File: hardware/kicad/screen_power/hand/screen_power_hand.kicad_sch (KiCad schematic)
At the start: 12 parts, among them J1 AUX 5V INPUT, J2 SCREEN CONTROL, Q1 2N3904

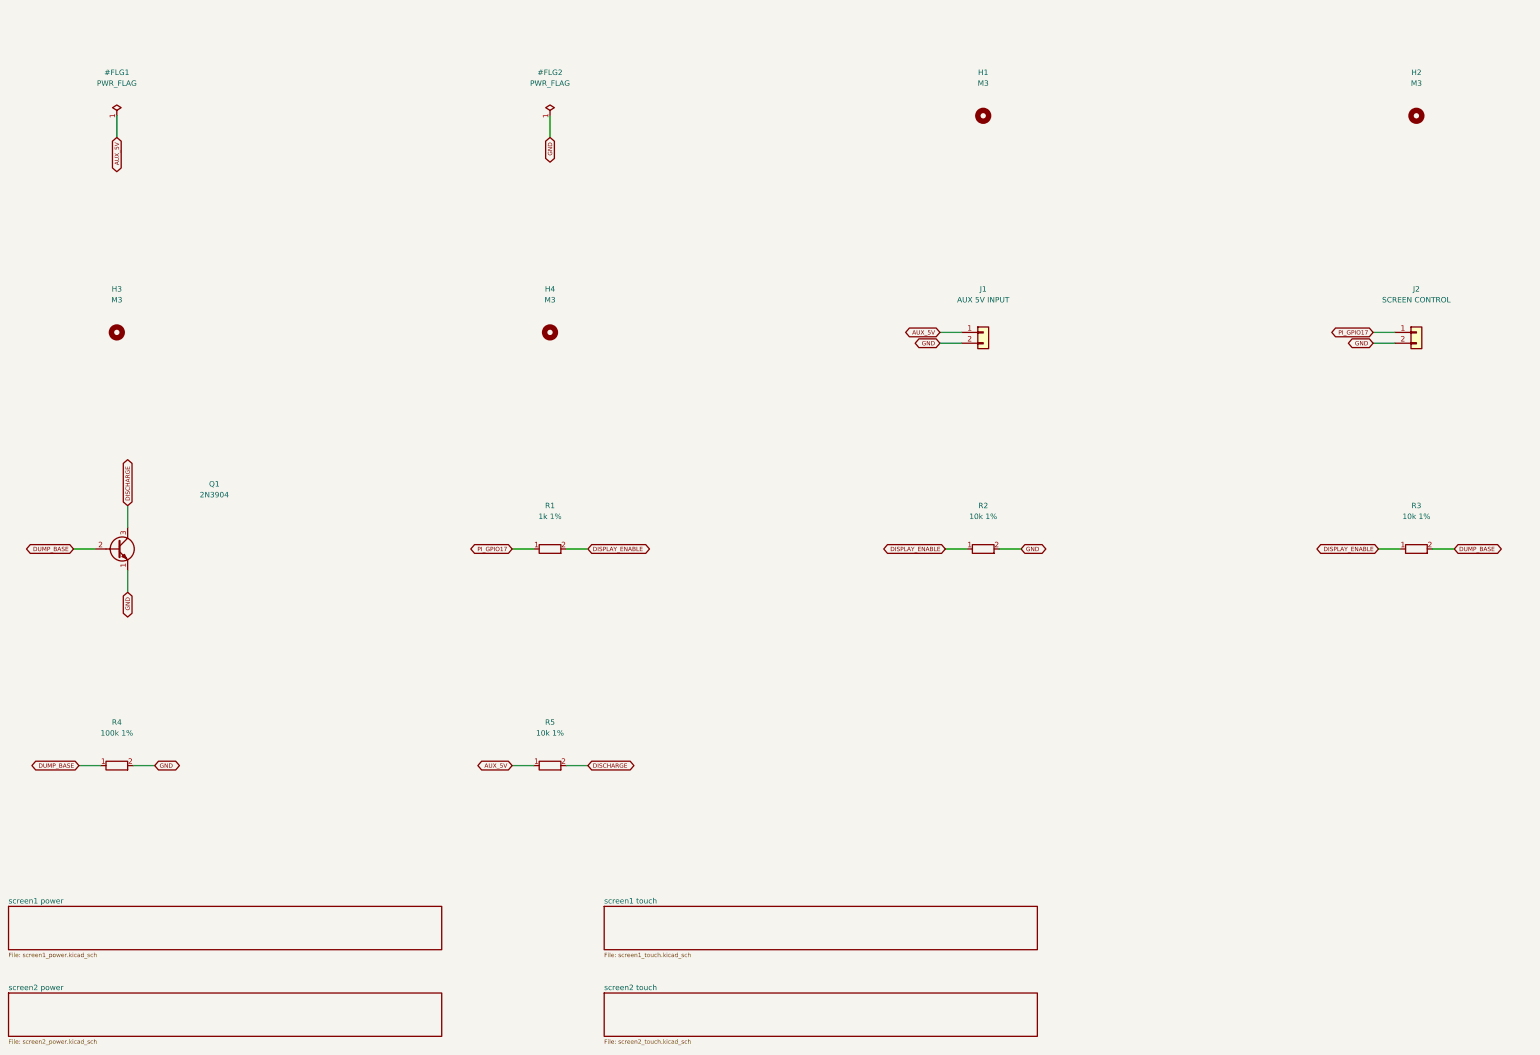
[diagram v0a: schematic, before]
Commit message: refactor(hardware): simplify and compact screen power boards
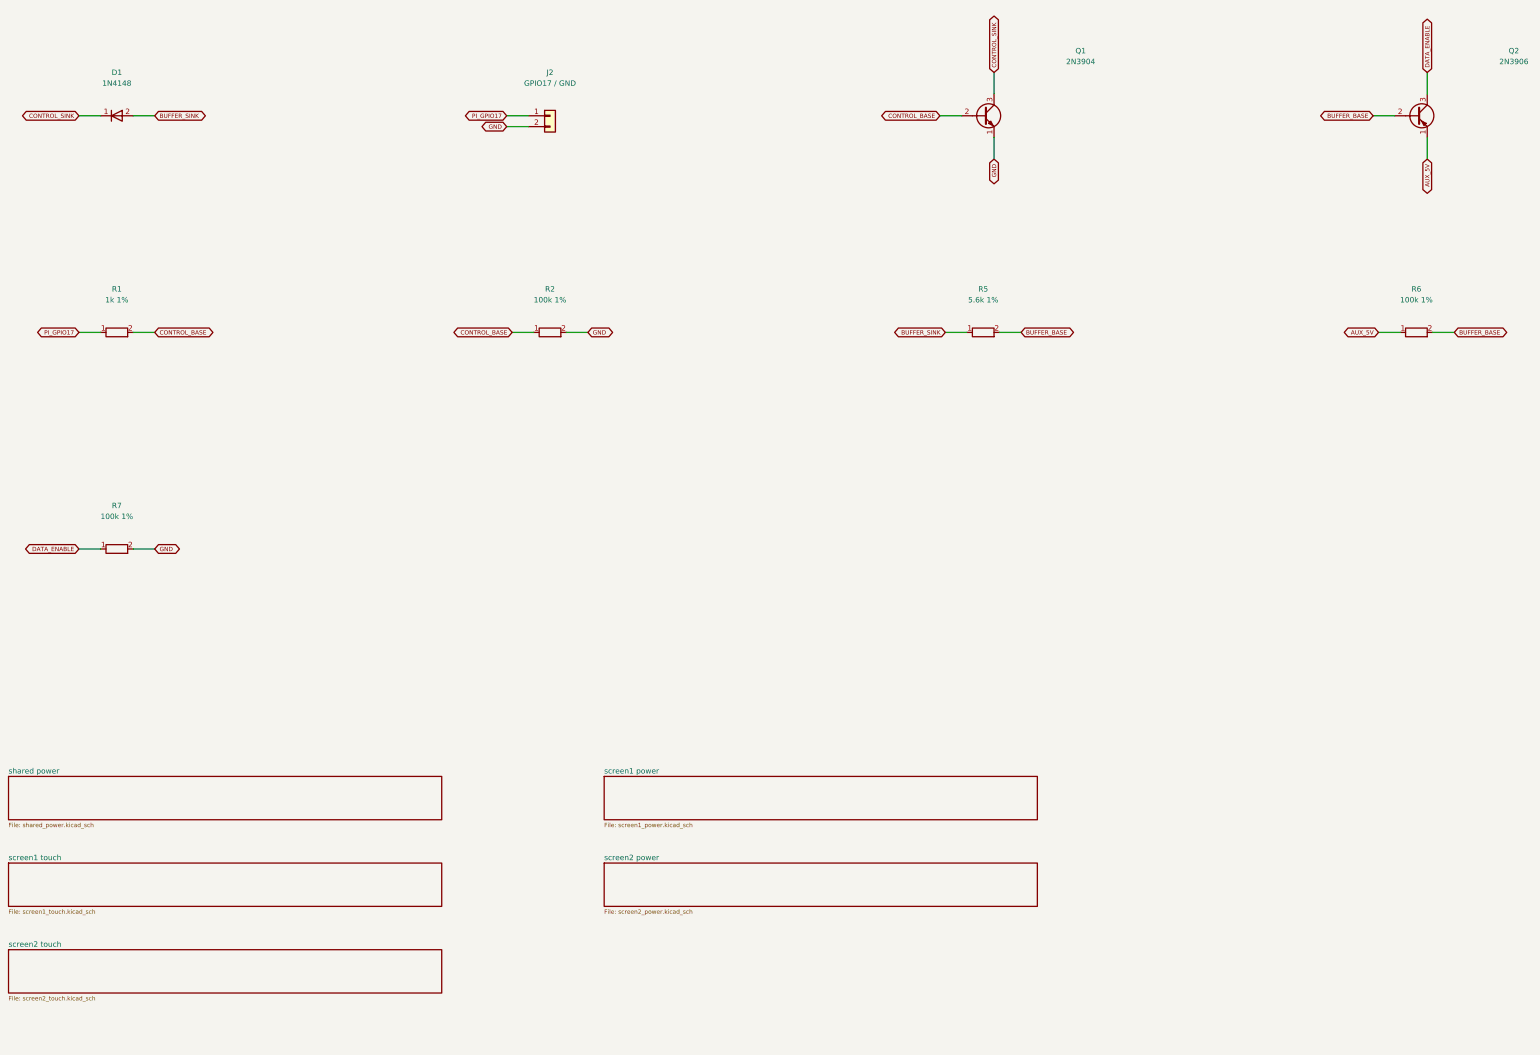
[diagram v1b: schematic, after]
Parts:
- removed H1, H2, H3, H4: M3, MountingHole:MountingHole_3.2mm_M3, symbol screen_symbols:Mechanical_MountingHole
- removed J1: AUX 5V INPUT, Connector_JST:JST_VH_B2P-VH_1x02_P3.96mm_Vertical, symbol screen_symbols:Connector_Generic_Conn_01x02
- removed R3: 10k 1%, Resistor_THT:R_Axial_DIN0207_L6.3mm_D2.5mm_P10.16mm_Horizontal, symbol screen_symbols:Device_R
- removed R4: 100k 1%, Resistor_THT:R_Axial_DIN0207_L6.3mm_D2.5mm_P10.16mm_Horizontal, symbol screen_symbols:Device_R
- added D1: 1N4148, Diode_THT:D_DO-35_SOD27_P7.62mm_Horizontal, symbol screen_symbols:Diode_1N4148
- added Q2: 2N3906, Package_TO_SOT_THT:TO-92_Inline_Wide, symbol screen_symbols:Transistor_BJT_2N3906
- added R6, R7: 100k 1%, Resistor_THT:R_Axial_DIN0207_L6.3mm_D2.5mm_P10.16mm_Horizontal, symbol screen_symbols:Device_R
- J2: value SCREEN CONTROL -> GPIO17 / GND
- R2: value 10k 1% -> 100k 1%; MPN MFR-25FBF52-10K -> MFR-25FBF52-100K
- R5: value 10k 1% -> 5.6k 1%; MPN MFR-25FBF52-10K -> MFR-25FBF52-5K6
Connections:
- net DUMP_BASE is gone; now on net CONTROL_BASE: Q1.2 (B)
- net AUX_5V: now also Q2.1 (E), R6.1; no longer R5.1
- net GND: now also R7.2
- net DISCHARGE renamed BUFFER_BASE
- net BUFFER_BASE: now also Q2.2 (B), R6.2; no longer Q1.3 (C)
- net DISPLAY_ENABLE renamed CONTROL_BASE
- new net BUFFER_SINK: D1.2 (A), R5.1
- new net CONTROL_SINK: D1.1 (K), Q1.3 (C)
- new net DATA_ENABLE: Q2.3 (C), R7.1
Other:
- added sheet shared power (shared_power.kicad_sch)
- moved on the sheet: J2, Q1, R1, R2, R5

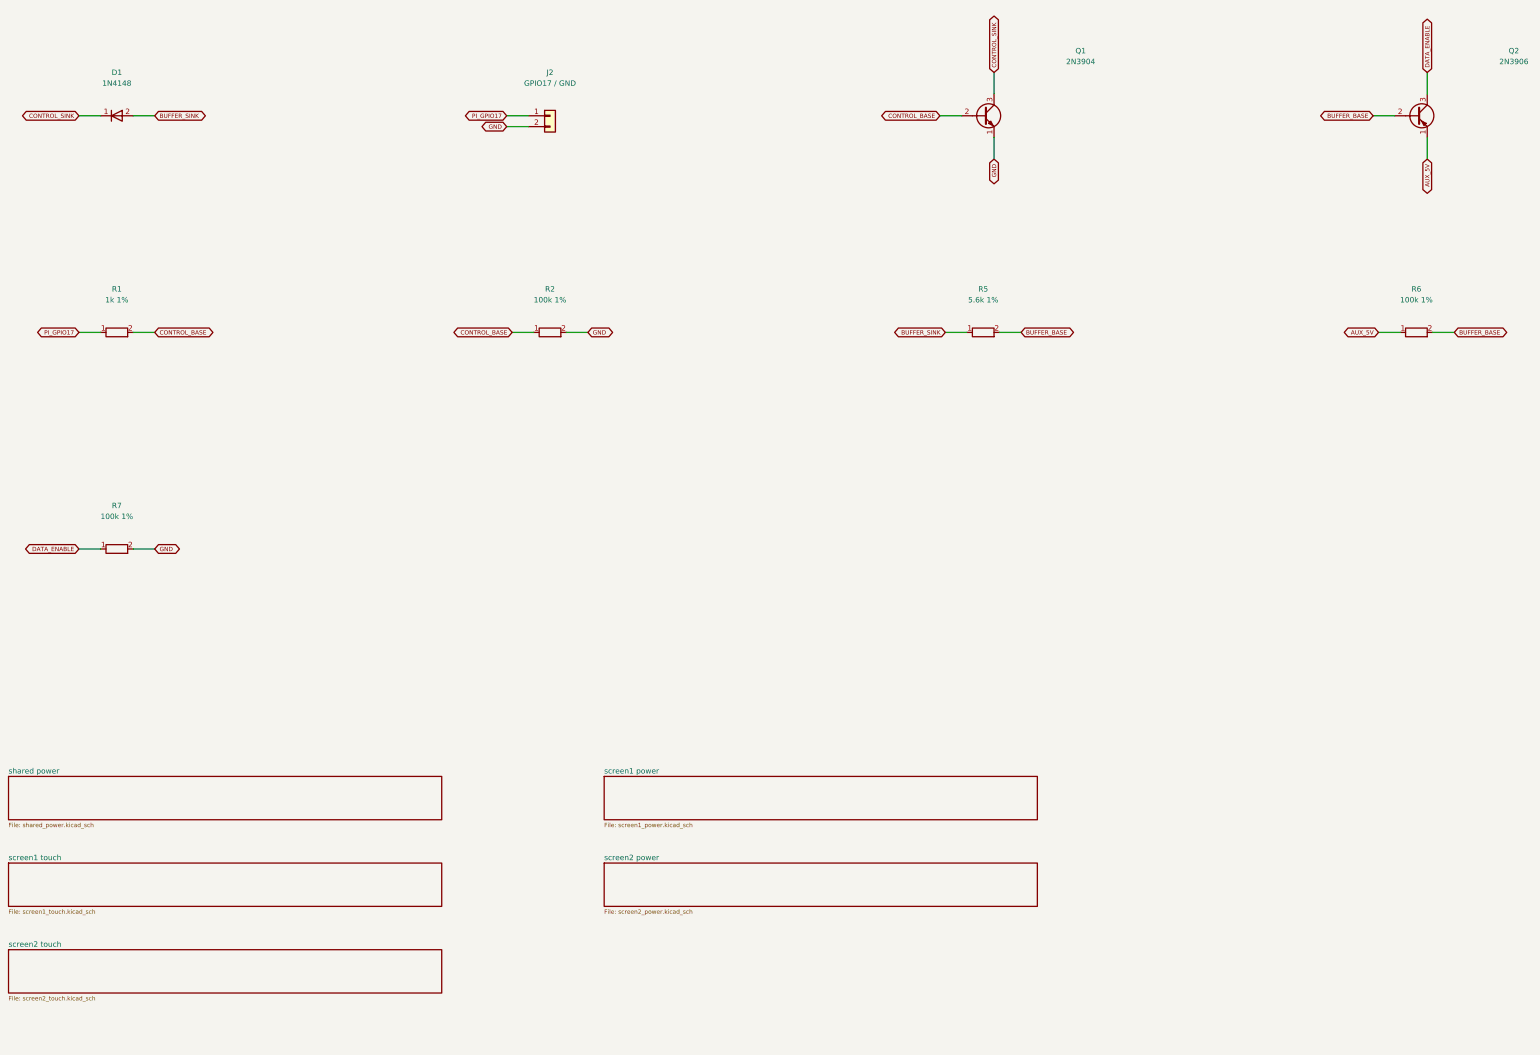
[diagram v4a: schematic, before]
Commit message: fix(hardware): strengthen screen gate drive and finish PCB copper
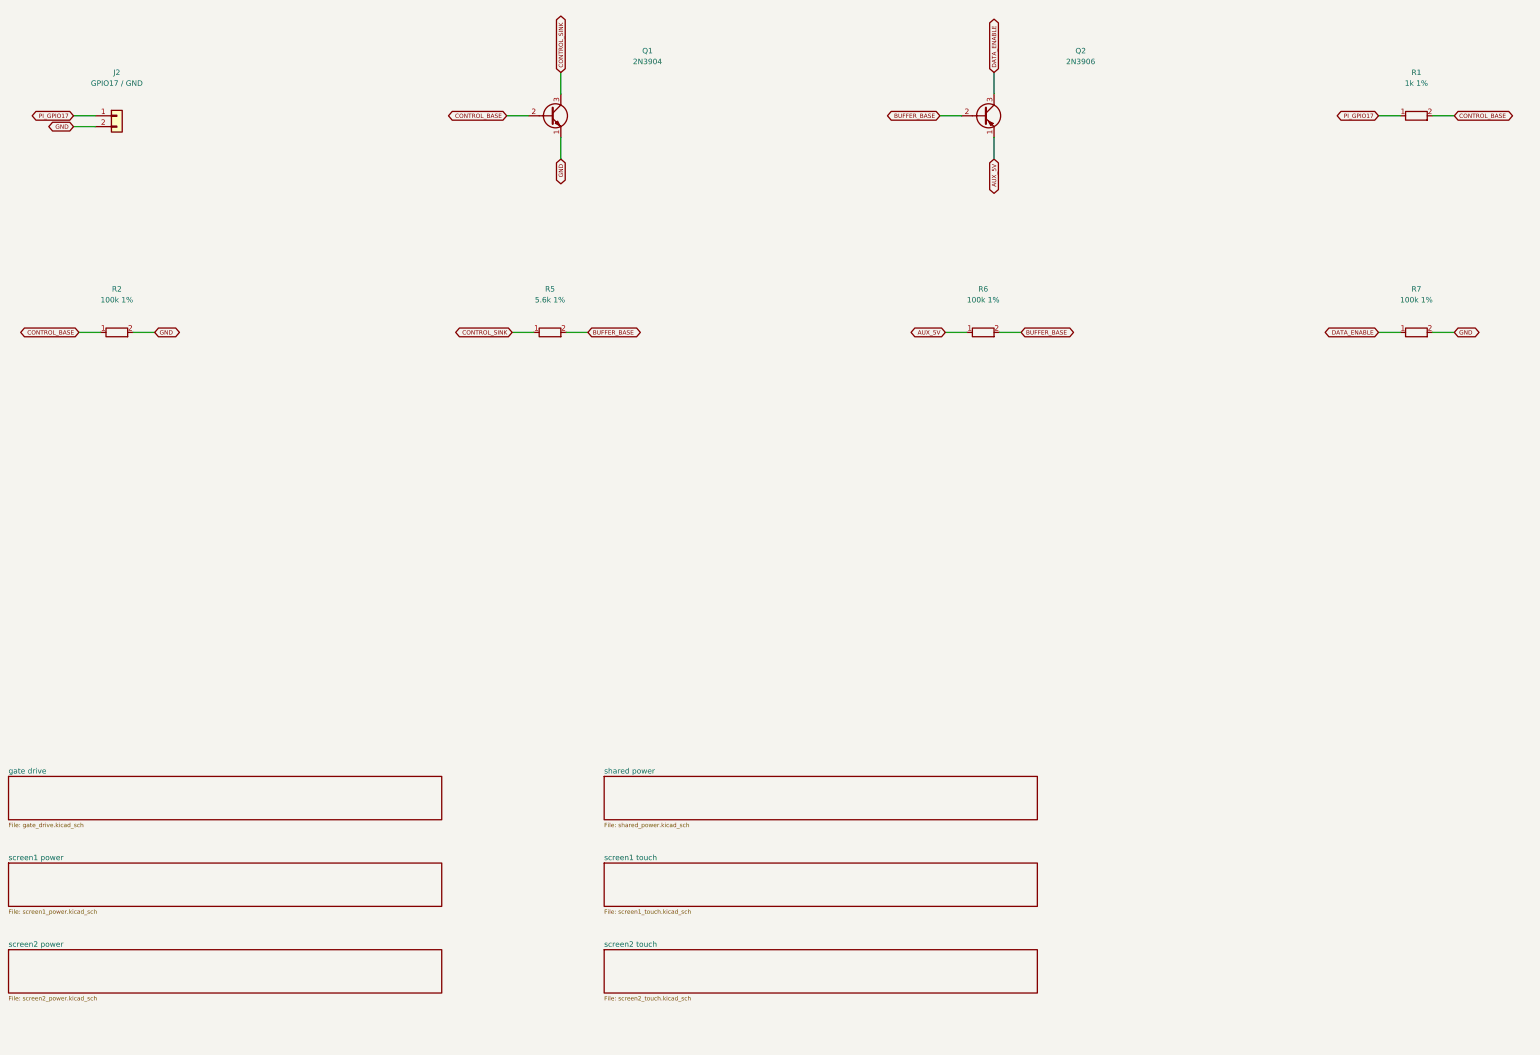
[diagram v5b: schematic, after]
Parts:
- removed D1: 1N4148, Diode_THT:D_DO-35_SOD27_P7.62mm_Horizontal, symbol screen_symbols:Diode_1N4148
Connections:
- net BUFFER_SINK is gone; now on net CONTROL_SINK: R5.1
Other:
- added sheet gate drive (gate_drive.kicad_sch)
- moved on the sheet: J2, Q1, Q2, R1, R2, R5, R6, R7

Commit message: fix(hardware): close Claude PCB review findings
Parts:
- R2: value 100k 1% -> 4.7k 1%; MPN MFR-25FBF52-100K -> MFR-25FBF52-4K7
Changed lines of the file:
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@@
         (font
           (size 1.27 1.27))))
-    (property "Value" "100k 1%"
+    (property "Value" "4.7k 1%"
       (at 50.8 106.68 90)
       (effects
@@
           (size 1.27 1.27))
         (hide yes)))
-    (property "MPN" "MFR-25FBF52-100K"
+    (property "MPN" "MFR-25FBF52-4K7"
       (at 50.8 114.3 90)
       (effects
